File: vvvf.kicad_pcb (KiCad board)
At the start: 2 copper layers, 5 parts, among them U1 TLP152, U3 HCPL-3120, U4 HCPL-3120, U5 HCPL-3120, U6 HCPL-3120

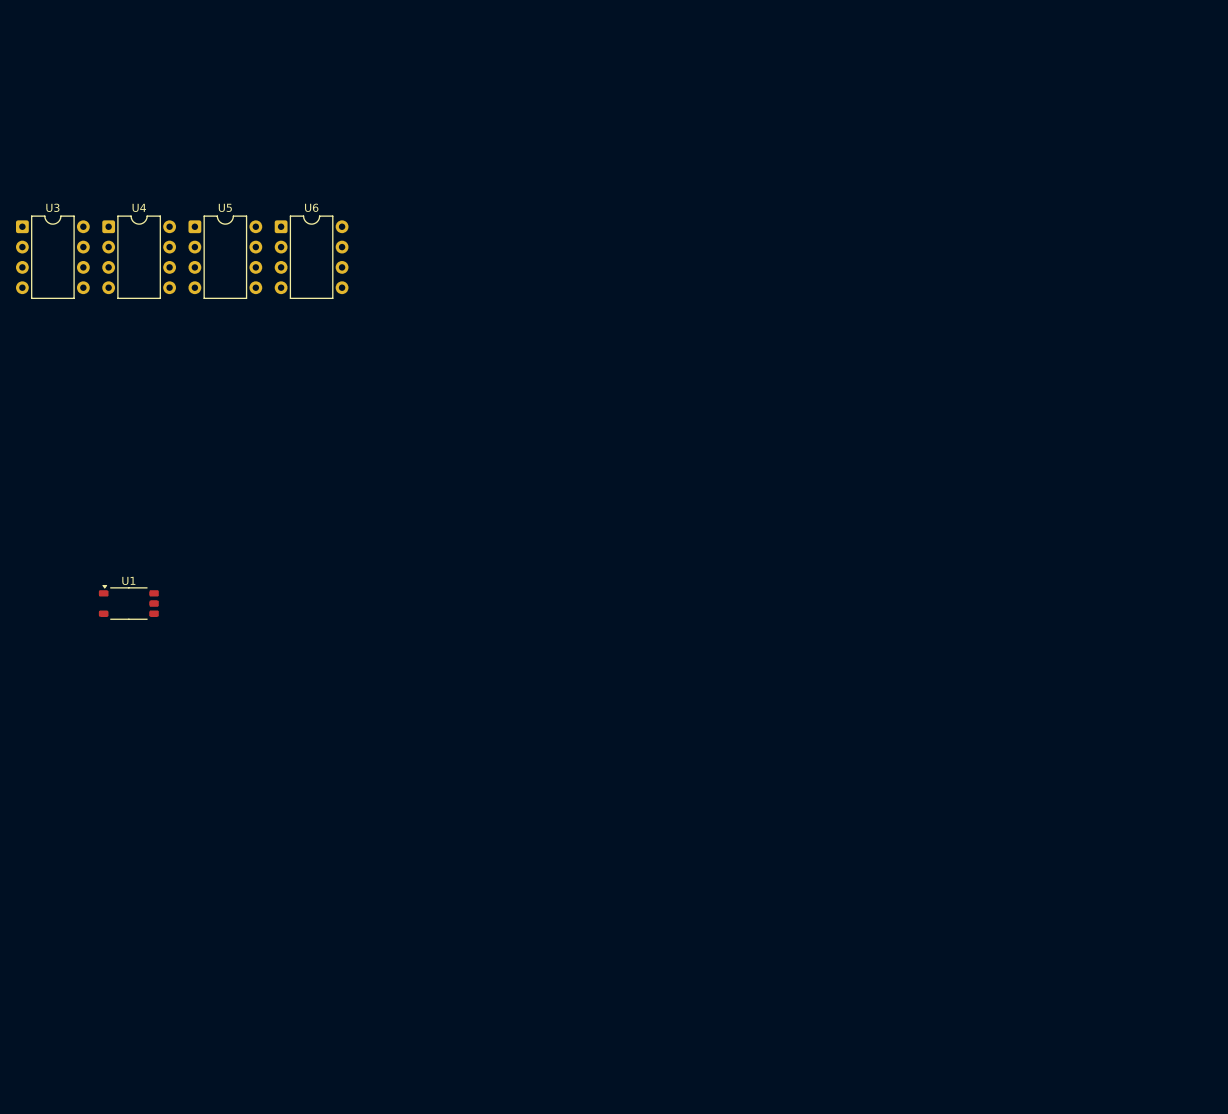
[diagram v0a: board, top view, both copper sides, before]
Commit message: Add rpico, couple other small things
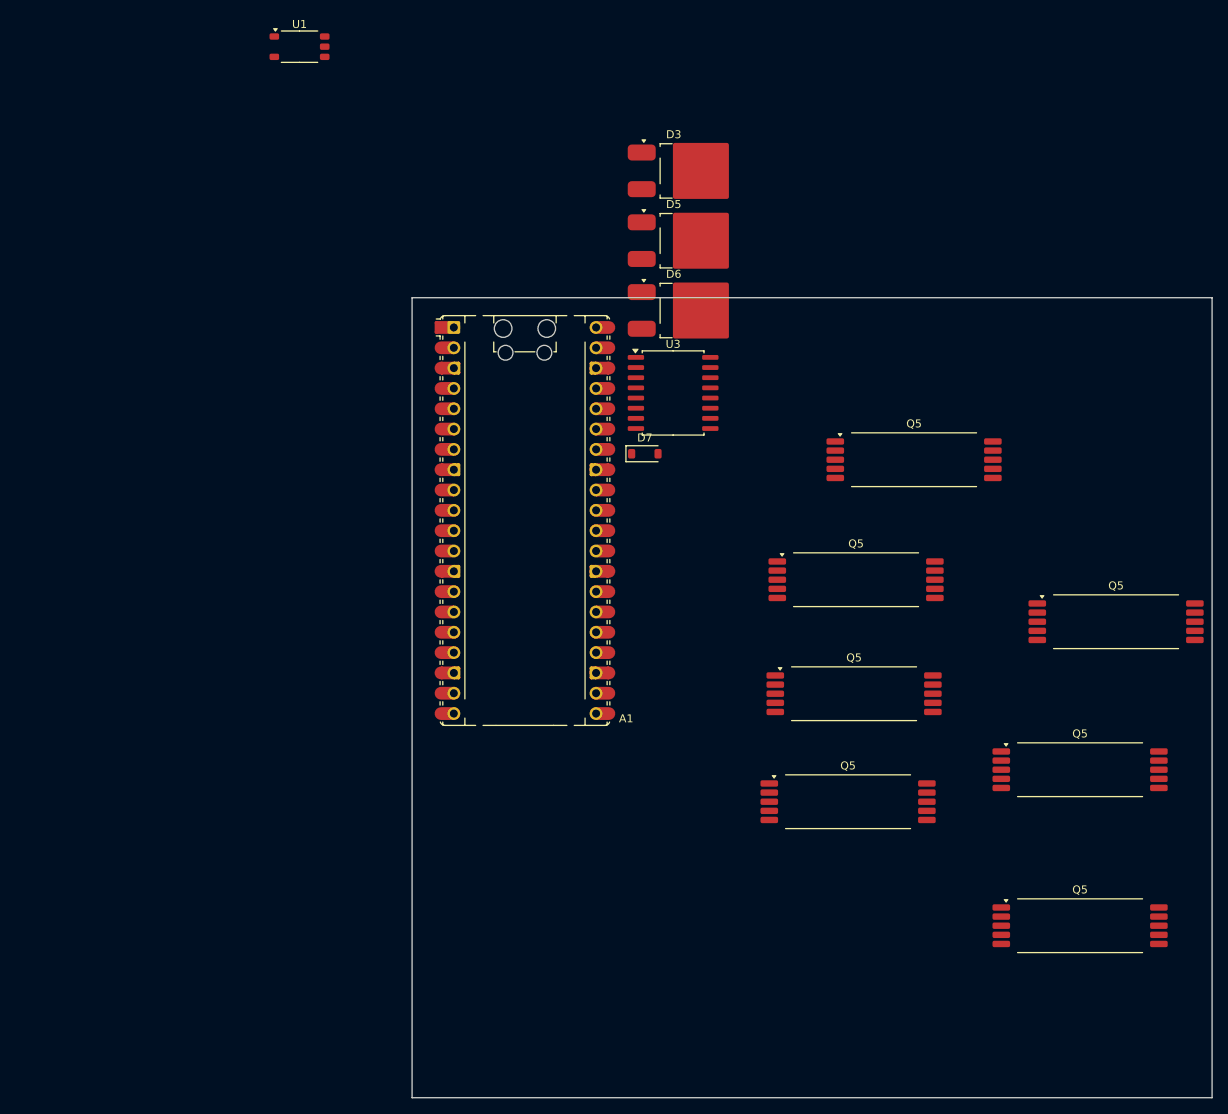
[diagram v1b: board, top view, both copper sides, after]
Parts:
- removed U4, U5, U6: HCPL-3120, Package_DIP:DIP-8_W7.62mm
- added A1: RaspberryPi_Pico, Module:RaspberryPi_Pico_Common_Unspecified, F.Cu at (154.1, 79.8)
- added D3: C4D02120E, Package_TO_SOT_SMD:TO-252-2_TabPin1, F.Cu at (174.1, 36.1)
- added D5: C4D02120E, Package_TO_SOT_SMD:TO-252-2_TabPin1, F.Cu at (174.1, 44.9)
- added D6: C4D02120E, Package_TO_SOT_SMD:TO-252-2_TabPin1, F.Cu at (174.1, 53.6)
- added D7: 1N4148W, Diode_SMD:D_SOD-123, F.Cu at (169.1, 71.5)
- added Q5: IPDD60R037CM8XTMA1, Package_TO_SOT_SMD:Infineon_PG-HDSOP-10-1, F.Cu at (195.5, 87.2)
- added Q5: IPDD60R037CM8XTMA1, Package_TO_SOT_SMD:Infineon_PG-HDSOP-10-1, F.Cu at (195.2, 101.5)
- added Q5: IPDD60R037CM8XTMA1, Package_TO_SOT_SMD:Infineon_PG-HDSOP-10-1, F.Cu at (223.5, 130.5)
- added Q5: IPDD60R037CM8XTMA1, Package_TO_SOT_SMD:Infineon_PG-HDSOP-10-1, F.Cu at (228.0, 92.5)
- added Q5: IPDD60R037CM8XTMA1, Package_TO_SOT_SMD:Infineon_PG-HDSOP-10-1, F.Cu at (202.8, 72.2)
- added Q5: IPDD60R037CM8XTMA1, Package_TO_SOT_SMD:Infineon_PG-HDSOP-10-1, F.Cu at (223.5, 111.0)
- added Q5: IPDD60R037CM8XTMA1, Package_TO_SOT_SMD:Infineon_PG-HDSOP-10-1, F.Cu at (194.5, 115.0)
- U3: value HCPL-3120 -> UCC21520ADW; footprint Package_DIP:DIP-8_W7.62mm -> Package_SO:SOIC-16W_7.5x10.3mm_P1.27mm
- moved U3 84.0 mm to (172.6, 63.9)
- moved U1 72.8 mm to (125.9, 20.6)
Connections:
- U3 pad 1: unconnected-(U3-NC-Pad1) -> GPXX
- U3 pad 2: Net-(U3-A) -> GPXX
- U3 pad 3: GND -> +5V
- U3 pad 4: unconnected-(U3-NC-Pad4) -> GND
- U3 pad 5: GND -> GPXX
- U3 pad 6: Net-(Q3-G) -> Net-(U3-DT)
- U3 pad 7: Net-(Q3-G) -> unconnected-(U3-NC-Pad7)
- U3 pad 8: +24V -> +5V
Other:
- board outline added: 100 x 100 mm

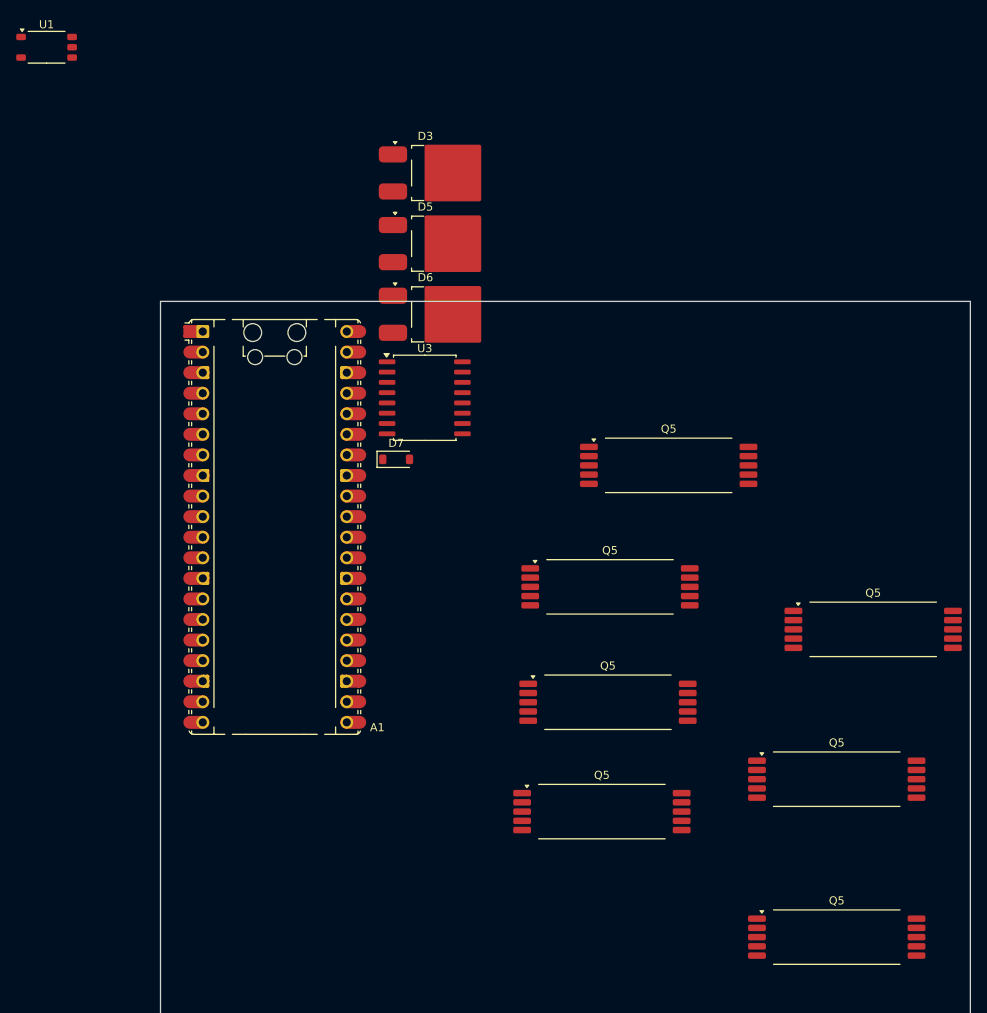
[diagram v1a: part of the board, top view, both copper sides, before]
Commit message: Add brake chopper
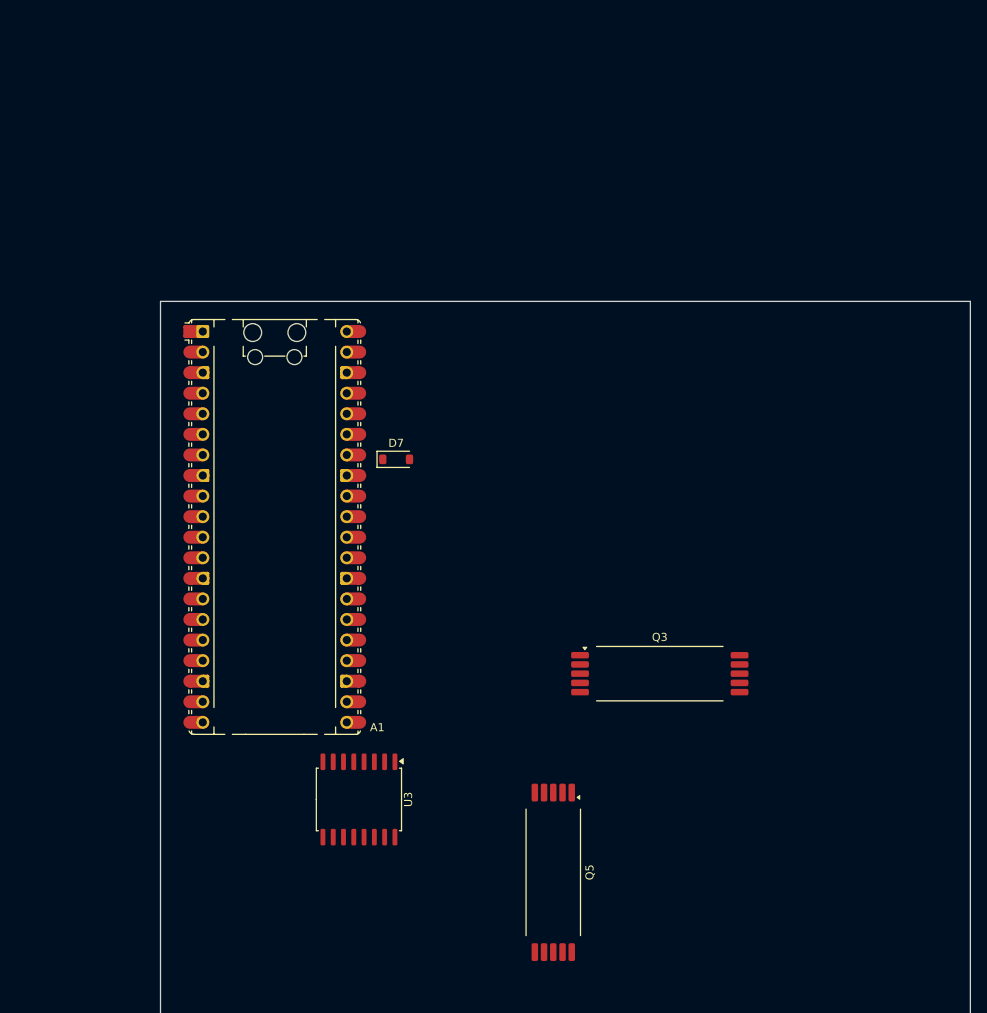
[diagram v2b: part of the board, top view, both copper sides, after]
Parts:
- removed D3, D5, D6: C4D02120E, Package_TO_SOT_SMD:TO-252-2_TabPin1
- removed the Q5 at (195.5, 87.2)
- removed the Q5 at (195.2, 101.5)
- removed the Q5 at (223.5, 130.5)
- removed the Q5 at (228.0, 92.5)
- removed the Q5 at (202.8, 72.2)
- removed the Q5 at (223.5, 111.0)
- removed U1: TLP152, Package_SO:SO-5-6_4.55x3.7mm_P1.27mm
- added Q3: IPDD60R037CM8XTMA1, Package_TO_SOT_SMD:Infineon_PG-HDSOP-10-1, F.Cu at (201.7, 98.0)
- moved U3 50.3 mm to (164.5, 113.5), turned to -90 degrees
- moved Q5 9.60 mm to (188.5, 122.5), turned to -90 degrees
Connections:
- net Net-(Q5-D-Pad10) renamed Vdrive
- A1 pad 33: unconnected-(A1-AGND-Pad33) -> GND
- Q5 pad 1: unconnected-(Q5-G-Pad1) -> Net-(D3-A)
- Q5 pad 2: unconnected-(Q5-DS-Pad2) -> Net-(Q5-DS)
- U3 pad 14: Net-(Q3-E) -> Net-(Q5-DS)

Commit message: Push changes at the end of the day
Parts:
- added C10: 100nF, Capacitor_SMD:C_0603_1608Metric_Pad1.08x0.95mm_HandSolder, F.Cu at (98.4, 129.0)
- added C11: 100nF, Capacitor_SMD:C_0603_1608Metric_Pad1.08x0.95mm_HandSolder, F.Cu at (98.4, 131.5)
- added C12: 1nF, Capacitor_SMD:C_0603_1608Metric_Pad1.08x0.95mm_HandSolder, F.Cu at (102.8, 113.9)
- added C13: 10uF, Capacitor_SMD:C_0603_1608Metric_Pad1.08x0.95mm_HandSolder, F.Cu at (102.8, 116.4)
- added C14: 10uF, Capacitor_SMD:C_0603_1608Metric_Pad1.08x0.95mm_HandSolder, F.Cu at (102.8, 119.0)
- added C15: 1uF, Capacitor_SMD:C_0603_1608Metric_Pad1.08x0.95mm_HandSolder, F.Cu at (102.8, 121.5)
- added C16: 100nF, Capacitor_SMD:C_0603_1608Metric_Pad1.08x0.95mm_HandSolder, F.Cu at (102.8, 124.0)
- added C17: 100nF, Capacitor_SMD:C_0603_1608Metric_Pad1.08x0.95mm_HandSolder, F.Cu at (102.8, 126.5)
- added C18: 1nF, Capacitor_SMD:C_0603_1608Metric_Pad1.08x0.95mm_HandSolder, F.Cu at (102.8, 129.0)
- added C19: 10uF, Capacitor_SMD:C_0603_1608Metric_Pad1.08x0.95mm_HandSolder, F.Cu at (102.8, 131.5)
- added C20: 10uF, Capacitor_SMD:C_0603_1608Metric_Pad1.08x0.95mm_HandSolder, F.Cu at (107.1, 113.9)
- added C21: 1uF, Capacitor_SMD:C_0603_1608Metric_Pad1.08x0.95mm_HandSolder, F.Cu at (107.1, 116.4)
- added C22: 100nF, Capacitor_SMD:C_0603_1608Metric_Pad1.08x0.95mm_HandSolder, F.Cu at (107.1, 119.0)
- added C4: 1nF, Capacitor_SMD:C_0603_1608Metric_Pad1.08x0.95mm_HandSolder, F.Cu at (98.4, 113.9)
- added C5: 10uF, Capacitor_SMD:C_0603_1608Metric_Pad1.08x0.95mm_HandSolder, F.Cu at (98.4, 116.4)
- added C6: 1uF, Capacitor_SMD:C_0603_1608Metric_Pad1.08x0.95mm_HandSolder, F.Cu at (98.4, 119.0)
- added C7: 100nF, Capacitor_SMD:C_0603_1608Metric_Pad1.08x0.95mm_HandSolder, F.Cu at (98.4, 121.5)
- added C8: 10uF, Capacitor_SMD:C_0603_1608Metric_Pad1.08x0.95mm_HandSolder, F.Cu at (98.4, 124.0)
- added C9: 100nF, Capacitor_SMD:C_0603_1608Metric_Pad1.08x0.95mm_HandSolder, F.Cu at (98.4, 126.5)
- added Q4: IPDD60R037CM8XTMA1, Package_TO_SOT_SMD:Infineon_PG-HDSOP-10-1, F.Cu at (160.8, 54.8)
- added Q6: IPDD60R037CM8XTMA1, Package_TO_SOT_SMD:Infineon_PG-HDSOP-10-1, F.Cu at (160.8, 62.8)
- added Q7: IPDD60R037CM8XTMA1, Package_TO_SOT_SMD:Infineon_PG-HDSOP-10-1, F.Cu at (160.8, 70.9)
- added Q8: IPDD60R037CM8XTMA1, Package_TO_SOT_SMD:Infineon_PG-HDSOP-10-1, F.Cu at (160.8, 78.9)
- added Q9: IPDD60R037CM8XTMA1, Package_TO_SOT_SMD:Infineon_PG-HDSOP-10-1, F.Cu at (160.8, 87.0)
- added R10: 10k, Resistor_SMD:R_0603_1608Metric_Pad0.98x0.95mm_HandSolder, F.Cu at (111.5, 113.9)
- added R11: 10, Resistor_SMD:R_0603_1608Metric_Pad0.98x0.95mm_HandSolder, F.Cu at (111.5, 116.4)
- added R12: 10k, Resistor_SMD:R_0603_1608Metric_Pad0.98x0.95mm_HandSolder, F.Cu at (111.5, 119.0)
- added R14: 10k, Resistor_SMD:R_0603_1608Metric_Pad0.98x0.95mm_HandSolder, F.Cu at (111.5, 121.5)
- added R16: 10k, Resistor_SMD:R_0603_1608Metric_Pad0.98x0.95mm_HandSolder, F.Cu at (111.5, 124.0)
- added R17: 2, Resistor_SMD:R_0603_1608Metric_Pad0.98x0.95mm_HandSolder, F.Cu at (111.5, 126.5)
- added R18: 10, Resistor_SMD:R_0603_1608Metric_Pad0.98x0.95mm_HandSolder, F.Cu at (111.5, 129.0)
- added R19: 10, Resistor_SMD:R_0603_1608Metric_Pad0.98x0.95mm_HandSolder, F.Cu at (111.5, 131.5)
- added R20: 10k, Resistor_SMD:R_0603_1608Metric_Pad0.98x0.95mm_HandSolder, F.Cu at (115.8, 113.9)
- added R21: 10k, Resistor_SMD:R_0603_1608Metric_Pad0.98x0.95mm_HandSolder, F.Cu at (115.8, 116.4)
- added R22: 10k, Resistor_SMD:R_0603_1608Metric_Pad0.98x0.95mm_HandSolder, F.Cu at (115.8, 119.0)
- added R23: 2, Resistor_SMD:R_0603_1608Metric_Pad0.98x0.95mm_HandSolder, F.Cu at (115.8, 121.5)
- added R24: 10, Resistor_SMD:R_0603_1608Metric_Pad0.98x0.95mm_HandSolder, F.Cu at (115.8, 124.0)
- added R25: 10, Resistor_SMD:R_0603_1608Metric_Pad0.98x0.95mm_HandSolder, F.Cu at (115.8, 126.5)
- added R26: 10k, Resistor_SMD:R_0603_1608Metric_Pad0.98x0.95mm_HandSolder, F.Cu at (115.8, 129.0)
- added R27: 10k, Resistor_SMD:R_0603_1608Metric_Pad0.98x0.95mm_HandSolder, F.Cu at (115.8, 131.5)
- added R3: 2, Resistor_SMD:R_0603_1608Metric_Pad0.98x0.95mm_HandSolder, F.Cu at (107.1, 121.5)
- added R4: 10k, Resistor_SMD:R_0603_1608Metric_Pad0.98x0.95mm_HandSolder, F.Cu at (107.1, 124.0)
- added R5: 10k, Resistor_SMD:R_0603_1608Metric_Pad0.98x0.95mm_HandSolder, F.Cu at (107.1, 126.5)
- added R6: 10, Resistor_SMD:R_0603_1608Metric_Pad0.98x0.95mm_HandSolder, F.Cu at (107.1, 129.0)
- added R9: 10, Resistor_SMD:R_0603_1608Metric_Pad0.98x0.95mm_HandSolder, F.Cu at (107.1, 131.5)
- added U5: ACS772ECB-400B-PFF-T, Snapeda:ACS772_PFF_ALM, F.Cu at (179.4, 74.2)
- added U6: UCC21520ADW, Package_SO:SOIC-16W_7.5x10.3mm_P1.27mm, F.Cu at (179.0, 81.8)
- added U7: UCC21520ADW, Package_SO:SOIC-16W_7.5x10.3mm_P1.27mm, F.Cu at (179.0, 93.7)
- moved A1 48.0 mm to (106.1, 77.8)
- moved D7 48.0 mm to (121.1, 69.5)
- moved Q3 48.0 mm to (153.7, 96.0)
- moved Q5 37.0 mm to (155.0, 106.8), turned to 0 degrees
- moved U3 10.1 mm to (174.5, 112.0)
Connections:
- A1 pad 1: unconnected-(A1-GPIO0-Pad1) -> /GP0
- A1 pad 10: unconnected-(A1-GPIO7-Pad10) -> /GP7
- A1 pad 11: unconnected-(A1-GPIO8-Pad11) -> /GP8
- A1 pad 12: unconnected-(A1-GPIO9-Pad12) -> /GP9
- A1 pad 14: unconnected-(A1-GPIO10-Pad14) -> /GP10
- A1 pad 15: unconnected-(A1-GPIO11-Pad15) -> /GP11
- A1 pad 16: unconnected-(A1-GPIO12-Pad16) -> /GP12
- A1 pad 17: unconnected-(A1-GPIO13-Pad17) -> /GP13
- A1 pad 19: unconnected-(A1-GPIO14-Pad19) -> /GP14
- A1 pad 2: unconnected-(A1-GPIO1-Pad2) -> /GP1
- A1 pad 20: unconnected-(A1-GPIO15-Pad20) -> /GP15
- A1 pad 21: unconnected-(A1-GPIO16-Pad21) -> /GP16
- A1 pad 22: unconnected-(A1-GPIO17-Pad22) -> /GP17
- A1 pad 24: unconnected-(A1-GPIO18-Pad24) -> /GP18
- A1 pad 25: unconnected-(A1-GPIO19-Pad25) -> /GP19
- A1 pad 26: unconnected-(A1-GPIO20-Pad26) -> /GP20
- A1 pad 27: unconnected-(A1-GPIO21-Pad27) -> /GP21
- A1 pad 29: unconnected-(A1-GPIO22-Pad29) -> /GP21
- A1 pad 31: unconnected-(A1-GPIO26_ADC0-Pad31) -> /ADC0
- A1 pad 32: unconnected-(A1-GPIO27_ADC1-Pad32) -> /ADC1
- A1 pad 34: unconnected-(A1-GPIO28_ADC2-Pad34) -> /ADC2
- A1 pad 4: unconnected-(A1-GPIO2-Pad4) -> /GP2
- A1 pad 5: unconnected-(A1-GPIO3-Pad5) -> /GP3
- A1 pad 6: unconnected-(A1-GPIO4-Pad6) -> /GP4
- A1 pad 7: unconnected-(A1-GPIO5-Pad7) -> /GP5
- A1 pad 9: unconnected-(A1-GPIO6-Pad9) -> /GP6
- U3 pad 1: GPXX -> /GP0
- U3 pad 2: GPXX -> /GP2

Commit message: Started with basic layout
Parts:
- added C23: 1uF, Snapeda:B32923C3105M000_CAPRR2250W80L2650T1100H2050, F.Cu at (220.0, 83.8)
- added C24: 100nF, Snapeda:B32922C3104K289_CAPRR1500W80L1800T500H1050, F.Cu at (203.0, 112.0)
- added C25: 1uF, Snapeda:B32923C3105M000_CAPRR2250W80L2650T1100H2050, F.Cu at (233.2, 108.5)
- added C26: 100nF, Snapeda:B32922C3104K289_CAPRR1500W80L1800T500H1050, F.Cu at (257.1, 99.5)
- added C27: 1uF, Snapeda:B32923C3105M000_CAPRR2250W80L2650T1100H2050, F.Cu at (28.8, 86.0)
- added C28: 100nF, Snapeda:B32922C3104K289_CAPRR1500W80L1800T500H1050, F.Cu at (76.8, 67.3)
- added C29: 1uF, Snapeda:B32923C3105M000_CAPRR2250W80L2650T1100H2050, F.Cu at (53.0, 94.8)
- added C30: 100nF, Snapeda:B32922C3104K289_CAPRR1500W80L1800T500H1050, F.Cu at (51.2, 82.8)
- added C31: 1uF, Snapeda:B32923C3105M000_CAPRR2250W80L2650T1100H2050, F.Cu at (53.0, 107.4)
- added C32: 100nF, Snapeda:B32922C3104K289_CAPRR1500W80L1800T500H1050, F.Cu at (76.8, 80.4)
- added C33: 1uF, Snapeda:B32923C3105M000_CAPRR2250W80L2650T1100H2050, F.Cu at (53.0, 120.0)
- added C34: 100nF, Snapeda:B32922C3104K289_CAPRR1500W80L1800T500H1050, F.Cu at (76.8, 87.0)
- added D10: ES1D, Diode_SMD:D_SMA_Handsoldering, B.Cu at (149.0, 108.8)
- added D11: ES1D, Diode_SMD:D_SMA_Handsoldering, B.Cu at (130.4, 109.1)
- added D12: ES1D, Diode_SMD:D_SMA_Handsoldering, B.Cu at (130.4, 113.4)
- added D13: ES1D, Diode_SMD:D_SMA_Handsoldering, B.Cu at (130.8, 130.2)
- added D15: ES1D, Diode_SMD:D_SMA_Handsoldering, F.Cu at (181.0, 93.0)
- added D3: ES1D, Diode_SMD:D_SMA_Handsoldering, B.Cu at (177.2, 130.8)
- added D5: ES1D, Diode_SMD:D_SMA_Handsoldering, B.Cu at (149.0, 130.8)
- added D6: ES1D, Diode_SMD:D_SMA_Handsoldering, B.Cu at (167.7, 161.9)
- added D8: ES1D, Diode_SMD:D_SMA_Handsoldering, B.Cu at (177.2, 108.6)
- added D9: ES1D, Diode_SMD:D_SMA_Handsoldering, F.Cu at (154.5, 93.2)
- C13, Q3, Q4, Q5, Q6, Q7, Q8, Q9, R18, R19, R6: moved to B.Cu
- R10, R20, R21, R5: value 10k -> 4.7k; moved to B.Cu
- R12, R16, R22, R26, R27, R4: value 10k -> 4.7k
- U5: value ACS772ECB-400B-PFF-T -> ACS770xCB-200B-PFF; footprint Snapeda:ACS772_PFF_ALM -> Sensor_Current:Allegro_CB_PFF
- moved Q4 109.6 mm to (150.4, 163.9), turned to 180 degrees
- moved U5 100.6 mm to (81.2, 95.7), turned to 180 degrees
- moved C7 82.7 mm to (177.0, 95.4), turned to 180 degrees
- moved C6 82.5 mm to (177.0, 93.6), turned to 180 degrees
- moved C5 82.3 mm to (177.0, 91.9), turned to 180 degrees
- moved C4 82.2 mm to (171.8, 76.8), turned to 90 degrees
- moved C8 78.8 mm to (170.3, 91.9), turned to 180 degrees
- moved R3 77.4 mm to (181.2, 99.2), turned to 90 degrees
- moved R6 75.8 mm to (180.2, 109.0), turned to -90 degrees
- moved C11 74.4 mm to (149.0, 76.9), turned to 90 degrees
- moved R10 71.8 mm to (180.0, 135.3), turned to -90 degrees
- moved R5 70.3 mm to (176.8, 116.3), turned to -90 degrees
- moved D7 66.0 mm to (187.0, 66.8), turned to 90 degrees
- moved U7 63.6 mm to (116.0, 85.2), turned to -90 degrees
- moved A1 61.3 mm to (165.5, 62.5), turned to -90 degrees
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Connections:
- C14 pad 2: Net-(Q6-DS) -> Net-(J2-Pin_1)
- C15 pad 2: Net-(Q6-DS) -> Net-(J2-Pin_1)
- C16 pad 2: Net-(Q6-DS) -> Net-(J2-Pin_1)
- C20 pad 2: Net-(Q8-DS) -> /C1
- C21 pad 2: Net-(Q8-DS) -> /C1
- C22 pad 2: Net-(Q8-DS) -> /C1
- C5 pad 2: Net-(Q5-DS) -> Net-(J1-Pin_1)
- C6 pad 2: Net-(Q5-DS) -> Net-(J1-Pin_1)
- C7 pad 2: Net-(Q5-DS) -> Net-(J1-Pin_1)
- Q5 pad 2: Net-(Q5-DS) -> Net-(J1-Pin_1)
- Q6 pad 2: Net-(Q6-DS) -> Net-(J2-Pin_1)
- Q8 pad 2: Net-(Q8-DS) -> /C1
- R16 pad 1: GPXX -> /GP14
- R20 pad 2: Net-(Q6-DS) -> Net-(J2-Pin_1)
- R22 pad 1: GPXX -> /GP15
- R26 pad 2: Net-(Q8-DS) -> /C1
- R4 pad 1: GPXX -> /GP13
- R5 pad 2: Net-(Q5-DS) -> Net-(J1-Pin_1)
- U3 pad 14: Net-(Q5-DS) -> Net-(J1-Pin_1)
- U3 pad 5: GPXX -> /GP13
- U5 pad 4: /C2 -> /C1
- U5 pad 5: /C1 -> /C2
- U6 pad 14: Net-(Q6-DS) -> Net-(J2-Pin_1)
- U6 pad 5: GPXX -> /GP14
- U7 pad 14: Net-(Q8-DS) -> /C1
- U7 pad 5: GPXX -> /GP15
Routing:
- net Net-(D3-K): track 0.00 -> 41.9 mm, vias 0 -> 1
- net Net-(J1-Pin_1): track 0.00 -> 33.9 mm
- net /C1: track 0.00 -> 21.3 mm
- net Net-(D8-K): track 0.00 -> 20.9 mm, vias 0 -> 1
- net Net-(D8-A): track 0.00 -> 11.2 mm
- net Net-(D15-K): track 0.00 -> 6.19 mm
- net Net-(D3-A): track 0.00 -> 4.68 mm
- net Net-(A1-VSYS): track 0.00 -> 3.01 mm
- net +24V: track 0.00 -> 2.80 mm
- net GNDPWR: track 0.00 -> 2.74 mm
- added copper zone on In2.Cu, net GNDPWR
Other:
- copper layers 2 -> 4
